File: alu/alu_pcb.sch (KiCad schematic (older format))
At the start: 0 parts

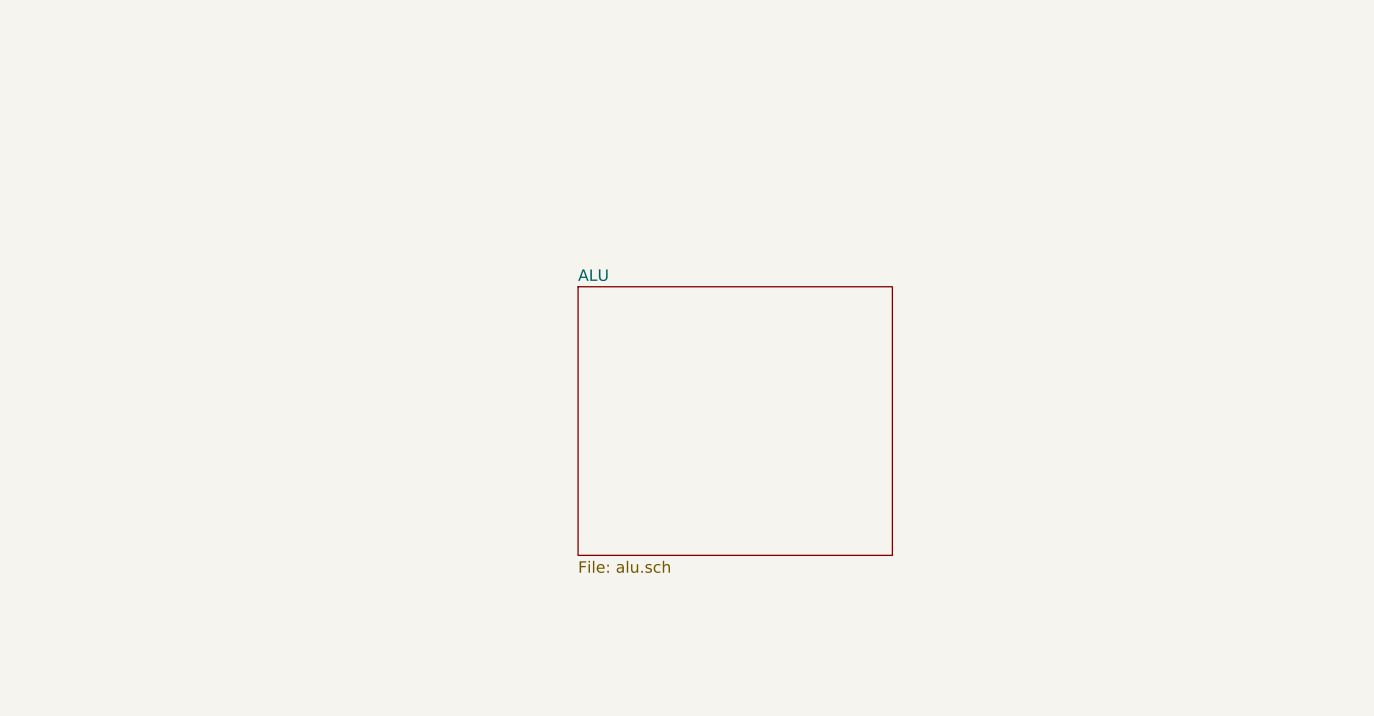
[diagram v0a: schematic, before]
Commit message: alu routed first iteration
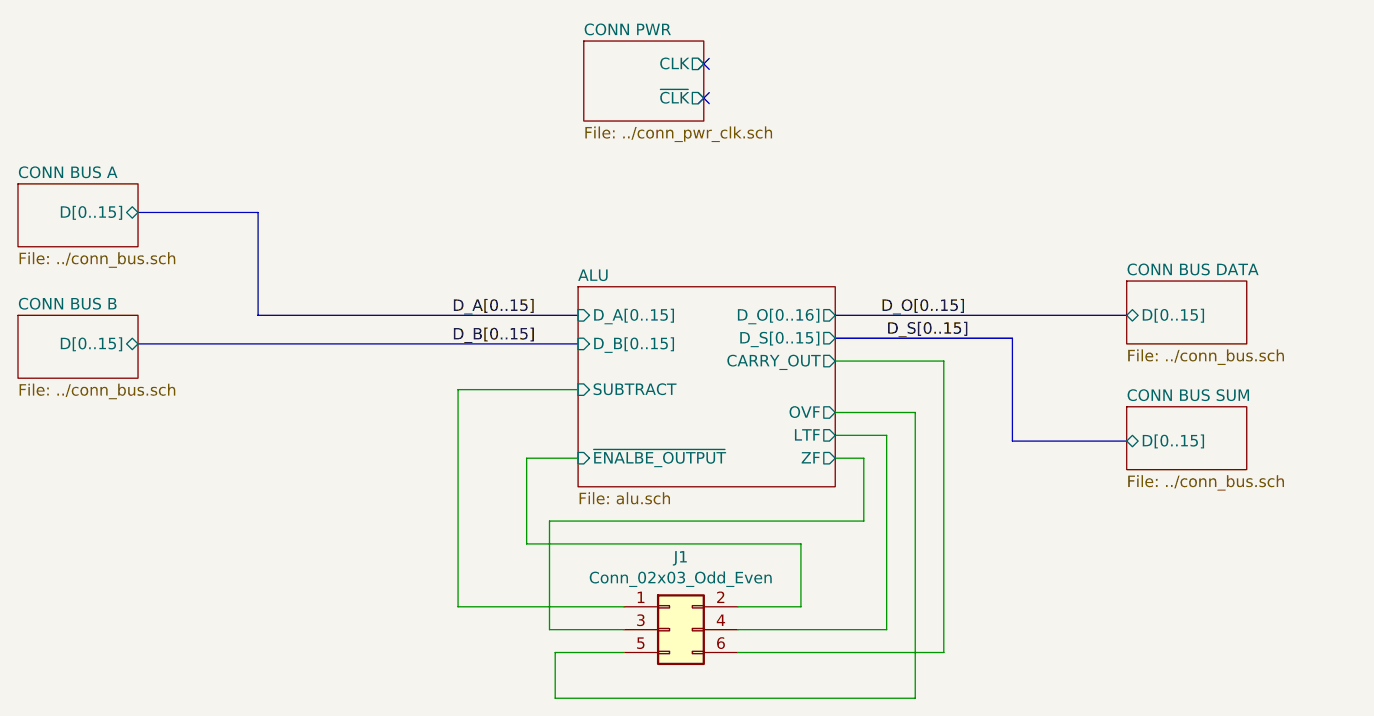
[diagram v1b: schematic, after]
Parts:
- added J1: Conn_02x03_Odd_Even, Connector_PinHeader_2.54mm:PinHeader_2x03_P2.54mm_Vertical, symbol Connector_Generic:Conn_02x03_Odd_Even
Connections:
- new net ALU/CARRY_OUT: J1.6 (Pin_6)
- new net ALU/LTF: J1.4 (Pin_4)
- new net ALU/OVF: J1.5 (Pin_5)
- new net ALU/SUBTRACT: J1.1 (Pin_1)
- new net ALU/ZF: J1.3 (Pin_3)
- new net ALU/~ENALBE_OUTPUT~: J1.2 (Pin_2)
- no-connect marks 0 -> 2
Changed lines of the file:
@@
 EESchema Schematic File Version 4
+LIBS:alu_pcb-cache
 EELAYER 30 0
 EELAYER END
 $Descr A4 11693 8268
 encoding utf-8
-Sheet 1 1
+Sheet 1 10
 Title ""
 Date ""
@@
 Comment4 ""
 $EndDescr
+Text Label 5650 2675 0    50   ~ 0
+D_A[0..15]
+Text Label 7525 2675 0    50   ~ 0
+D_O[0..15]
 $Sheet
-S 6200 2550 1375 1175
+S 6225 1475 525  350
+U 5EEF511D
+F0 "CONN PWR" 50
+F1 "../conn_pwr_clk.sch" 50
+F2 "CLK" O R 6750 1575 50
+F3 "~CLK~" O R 6750 1725 50
+$EndSheet
+NoConn ~ 6750 1725
+NoConn ~ 6750 1575
+$Sheet
+S 3750 2100 525  275
+U 5EF00B1E
+F0 "CONN BUS A" 50
+F1 "../conn_bus.sch" 50
+F2 "D[0..15]" B R 4275 2225 50
+$EndSheet
+$Sheet
+S 3750 2675 525  275
+U 5EF08E50
+F0 "CONN BUS B" 50
+F1 "../conn_bus.sch" 50
+F2 "D[0..15]" B R 4275 2800 50
+$EndSheet
+Text Label 5650 2800 0    50   ~ 0
+D_B[0..15]
+Wire Bus Line
+	4800 2675 4800 2225
+Wire Bus Line
+	4800 2225 4275 2225
+Wire Bus Line
+	4800 2675 6200 2675
+$Sheet
+S 8600 2525 525  275
+U 5EF0F599
+F0 "CONN BUS DATA" 50
+F1 "../conn_bus.sch" 50
+F2 "D[0..15]" B L 8600 2675 50
+$EndSheet
+Wire Bus Line
+	7325 2675 8600 2675
+$Comp
+L Connector_Generic:Conn_02x03_Odd_Even J1
+U 1 1 5EF11C7B
+P 6600 4050
+F 0 "J1" H 6650 4367 50  0000 C CNN
+F 1 "Conn_02x03_Odd_Even" H 6650 4276 50  0000 C CNN
+F 2 "Connector_PinHeader_2.54mm:PinHeader_2x03_P2.54mm_Vertical" H 6600 4050 50  0001 C CNN
+F 3 "~" H 6600 4050 50  0001 C CNN
+	1    6600 4050
+	1    0    0    -1
+$EndComp
+Wire Wire Line
+	6200 3000 5675 3000
+Wire Wire Line
+	6200 3300 5975 3300
+Wire Wire Line
+	7175 3675 7175 3950
+Wire Wire Line
+	7175 3950 6900 3950
+Wire Wire Line
+	6075 3575 6075 4050
+Wire Wire Line
+	7325 3100 7675 3100
+Wire Wire Line
+	6100 4350 6100 4150
+Wire Wire Line
+	6100 4150 6400 4150
+Wire Wire Line
+	7450 3575 7450 3300
+Wire Wire Line
+	6075 3575 7450 3575
+Wire Wire Line
+	7325 2875 7800 2875
+Wire Bus Line
+	4275 2800 6200 2800
+Wire Wire Line
+	6900 4050 7550 4050
+Wire Wire Line
+	7550 3200 7550 4050
+Wire Wire Line
+	6075 4050 6400 4050
+Wire Wire Line
+	7325 3300 7450 3300
+$Sheet
+S 6200 2550 1125 875
 U 5EBD9EFC
 F0 "ALU" 50
 F1 "alu.sch" 50
+F2 "D_A[0..15]" I L 6200 2675 50
+F3 "D_B[0..15]" I L 6200 2800 50
+F4 "~ENALBE_OUTPUT~" I L 6200 3300 50
+F5 "CARRY_OUT" O R 7325 2875 50
+F6 "D_O[0..16]" O R 7325 2675 50
+F7 "SUBTRACT" I L 6200 3000 50
+F8 "ZF" O R 7325 3300 50
+F9 "LTF" O R 7325 3200 50
+F10 "OVF" O R 7325 3100 50
+F11 "D_S[0..15]" O R 7325 2775 50
 $EndSheet
+Wire Wire Line
+	7325 3200 7550 3200
+$Sheet
+S 8600 3075 525  275
+U 5ED21DE0
+F0 "CONN BUS SUM" 50
+F1 "../conn_bus.sch" 50
+F2 "D[0..15]" B L 8600 3225 50
+$EndSheet
+Wire Bus Line
+	7325 2775 8100 2775
+Wire Bus Line
+	8100 2775 8100 3225
+Wire Bus Line
+	8100 3225 8600 3225
+Text Label 7550 2775 0    50   ~ 0
+D_S[0..15]
+Wire Wire Line
+	7800 2875 7800 4150
+Wire Wire Line
+	6900 4150 7800 4150
+Wire Wire Line
+	7675 3100 7675 4350
+Wire Wire Line
+	6100 4350 7675 4350
+Wire Wire Line
+	5675 3950 6400 3950
+Wire Wire Line
+	5675 3000 5675 3950
+Wire Wire Line
+	5975 3300 5975 3675
+Wire Wire Line
+	5975 3675 7175 3675
 $EndSCHEMATC
